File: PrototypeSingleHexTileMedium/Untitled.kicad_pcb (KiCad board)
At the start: 2 copper layers, 44 x 38.1 mm, 12 parts

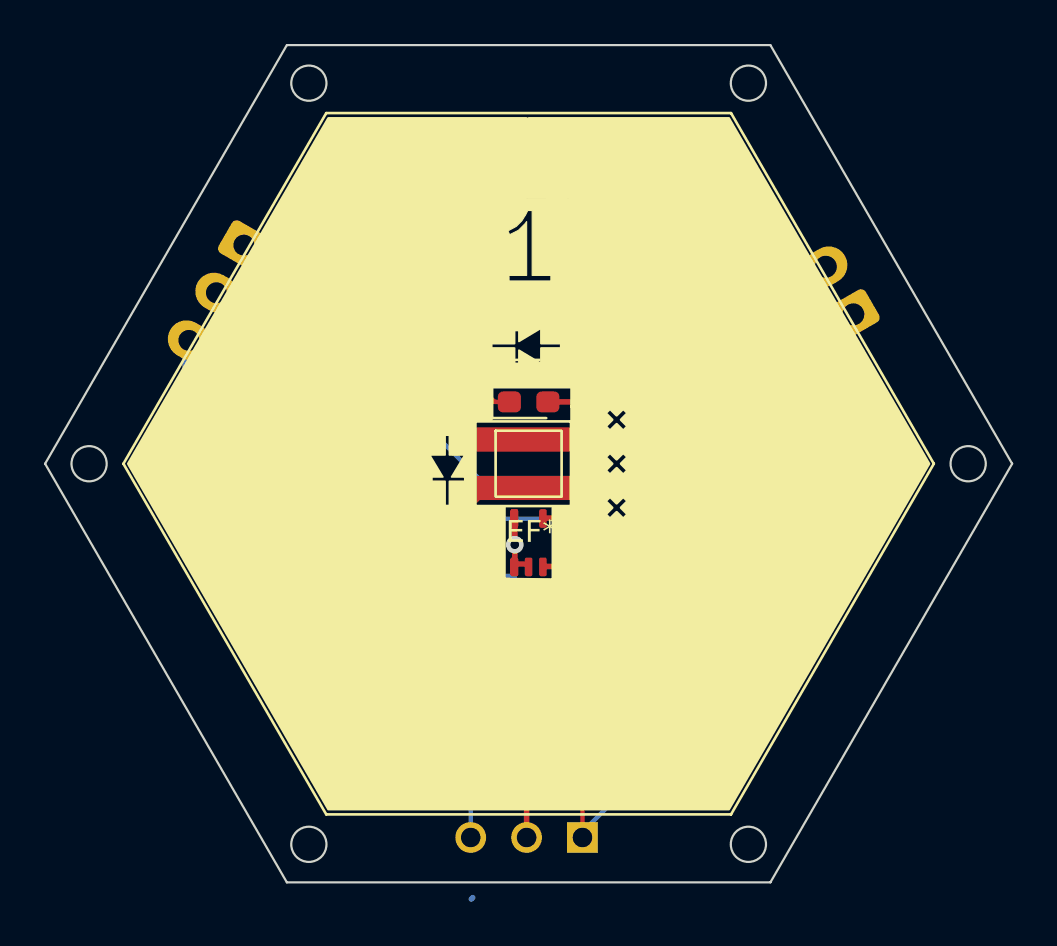
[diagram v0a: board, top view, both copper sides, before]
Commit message: v5 of the prototype hexboard and squareboards:  added label to capacitors and resistors; moved temperature sensors to periphery; added 0.1 mm back to top and bottom of boards
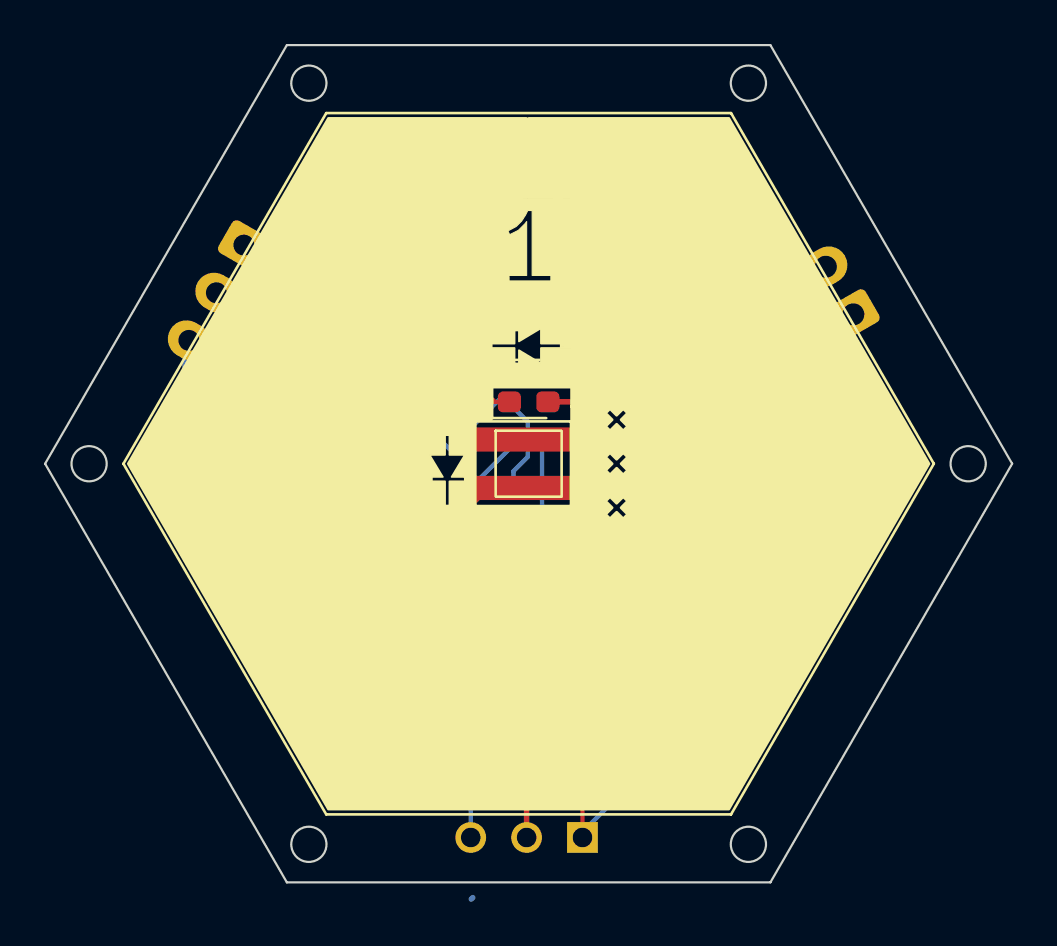
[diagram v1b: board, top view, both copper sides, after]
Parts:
- removed ? (x2): , 
- REF**: moved to B.Cu
- REF**: value R_0402_1005Metric -> R_1206_3216Metric; footprint Resistor_SMD:R_0402_1005Metric -> Resistor_SMD:R_1206_3216Metric
- moved REF** 3.60 mm to (103.7, 58.0), turned to 180 degrees
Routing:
- net (no net): track 229.2 -> 229.8 mm, vias 4 -> 1
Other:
- board text added: "Designed by Sebouh J. Paul v2 sidelength=21.98 mm"
- board text removed: "Designed by Sebouh J. Paul v1 sidelength=21.98 mm"
